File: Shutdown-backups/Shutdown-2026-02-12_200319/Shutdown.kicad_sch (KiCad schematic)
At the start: 69 parts, among them J1 0194270049, J2 0194270049, Q1 AO3400A, Q10 SI2318CDS-T1-GE3, Q11 SI2347DS-T1-GE3, Q2 AO3400A, Q3 AO3400A, Q4 SI2347DS-T1-GE3, Q5 AO3400A, Q6 AO3400A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

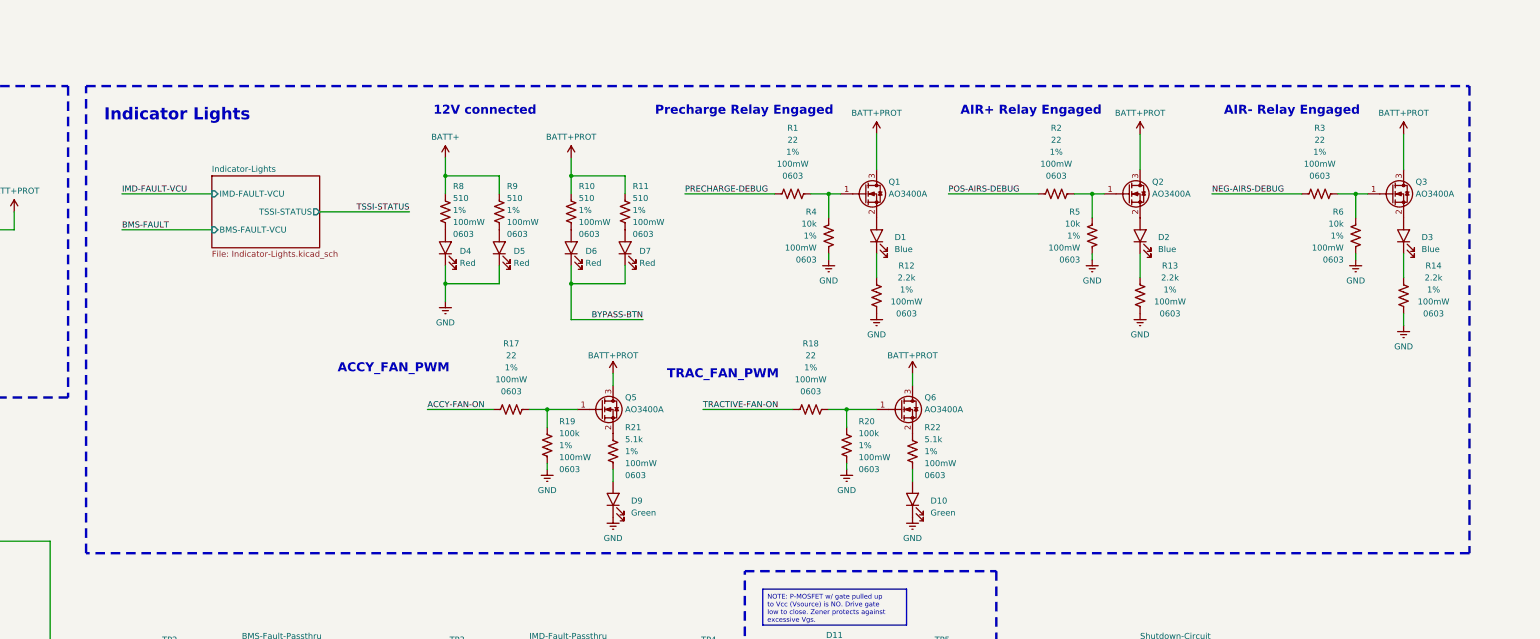
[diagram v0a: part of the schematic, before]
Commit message: Finished shutdown, 0 drc, need to export gerbers
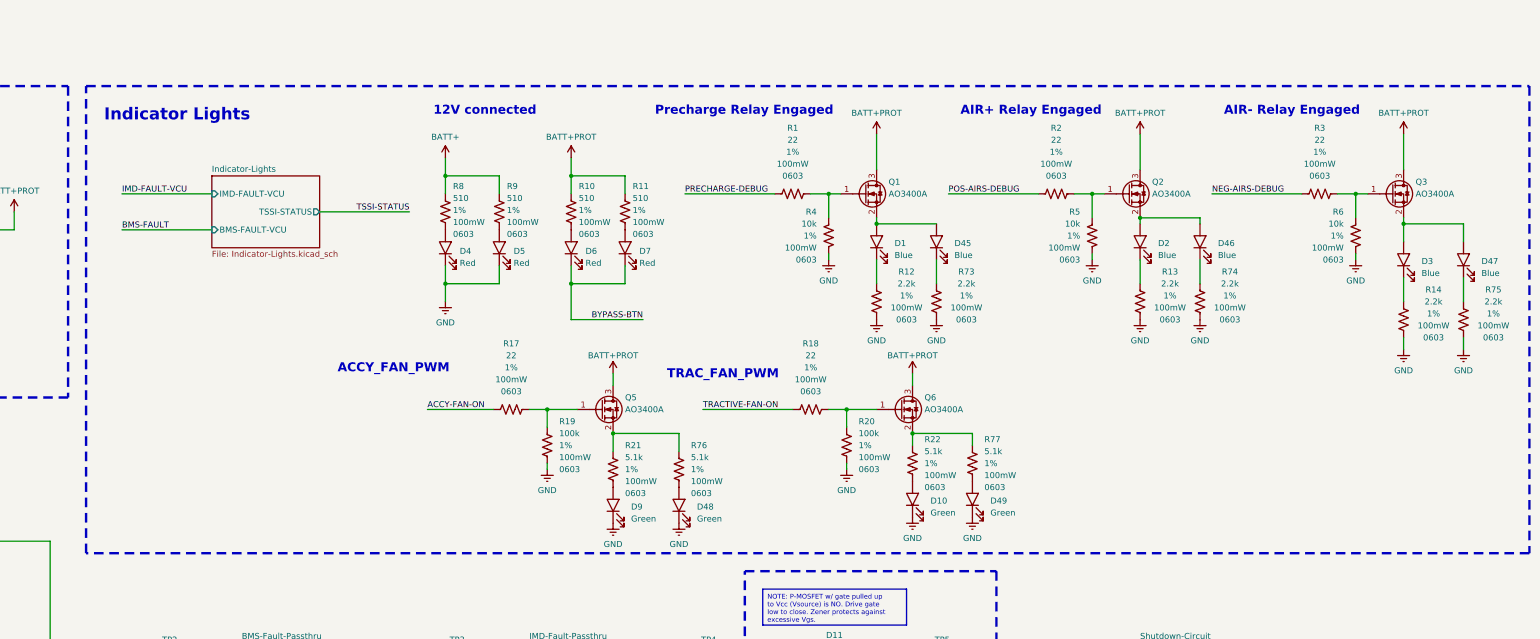
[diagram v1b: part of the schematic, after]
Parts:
- added D45, D46, D47: Blue, LED_SMD:LED_0805_2012Metric, symbol -Diodes-LED:NCD0805B2
- added D48, D49: Green, LED_SMD:LED_0805_2012Metric, symbol -Diodes-LED:NCD0805G1
- added R73, R74, R75: 2.2k, Resistor_SMD:R_0603_1608Metric_Pad0.98x0.95mm_HandSolder, symbol -R-SMD-0603:R-0603-2.2k-1%-100mW-100PPM
- added R76, R77: 5.1k, Resistor_SMD:R_0603_1608Metric_Pad0.98x0.95mm_HandSolder, symbol -R-SMD-0603:R-0603-5.1k-1%-100mW-100PPM_1_1
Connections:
- net GND: now also D48.1 (K), D49.1 (K), R73.2, R74.2, R75.2
- net at D1.2 (A), Q1.2 (S): now also D45.2 (A)
- net at D2.2 (A), Q2.2 (S): now also D46.2 (A)
- net at Q6.2 (S), R22.2: now also R77.2
- net at D3.2 (A), Q3.2 (S): now also D47.2 (A)
- net at Q5.2 (S), R21.2: now also R76.2
- new net: D48.2 (A), R76.1
- new net: D46.1 (K), R74.1
- new net: D49.2 (A), R77.1
- new net: D47.1 (K), R75.1
- new net: D45.1 (K), R73.1
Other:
- moved on the sheet: D1, D2, D3, D9, R12, R13, R14, R21, R22
